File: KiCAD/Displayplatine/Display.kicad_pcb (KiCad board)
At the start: 2 copper layers, 14 parts, among them P1 CONN_01X08

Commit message: Displayplatine fertig + EADOG Footprint korrigiert
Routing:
- net GND: track 0.00 -> 267.9 mm
- net VCC: track 0.00 -> 93.5 mm
- net D5: track 0.00 -> 67.6 mm
- net D4: track 0.00 -> 67.6 mm
- net D3: track 0.00 -> 67.6 mm
- net D2: track 0.00 -> 67.6 mm
- net D1: track 0.00 -> 67.6 mm
- net Net-(C2-Pad1): track 0.00 -> 26.6 mm
- net LED: track 0.00 -> 24.4 mm
- net Net-(C5-Pad2): track 0.00 -> 19.2 mm
- net Net-(C7-Pad2): track 0.00 -> 14.1 mm
- net Net-(C3-Pad2): track 0.00 -> 13.6 mm
- net Net-(C1-Pad2): track 0.00 -> 13.6 mm
- net Net-(C2-Pad2): track 0.00 -> 12.2 mm
- net Net-(C6-Pad2): track 0.00 -> 11.7 mm
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
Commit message: nochmal
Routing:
- net VCC: track 93.5 -> 89.2 mm
- net GND: track 267.9 -> 266.5 mm
- added copper zone on B.Cu, net GND
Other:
- board outline added: 92.7 x 76.2 mm
- net class Default: trace_width 0.25 -> 0.3

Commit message: Displayplatine fertig
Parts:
- added P2: CONN_01X01, Pin_Headers:Pin_Header_Straight_1x01, F.Cu at (166.4, 123.2)
- added P3: CONN_01X01, Pin_Headers:Pin_Header_Straight_1x01, F.Cu at (166.4, 57.1)
- added P4: CONN_01X01, Pin_Headers:Pin_Header_Straight_1x01, F.Cu at (81.3, 57.1)
- added P5: CONN_01X01, Pin_Headers:Pin_Header_Straight_1x01, F.Cu at (81.3, 123.2)
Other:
- board size 92.7 x 76.2 mm -> 92.7 x 73.7 mm
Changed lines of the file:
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@@
     (links 36)
     (no_connects 0)
-    (area 81.35051 58.094999 158.145 118.435002)
+    (area 77.394999 53.264999 170.255001 127.075001)
     (thickness 1.6)
     (drawings 5)
     (tracks 115)
     (zones 0)
-    (modules 14)
-    (nets 23)
+    (modules 18)
+    (nets 27)
   )
   (page A4)
@@
   (net 21 D4)
   (net 22 LED)
+  (net 23 "Net-(P2-Pad1)")
+  (net 24 "Net-(P3-Pad1)")
+  (net 25 "Net-(P4-Pad1)")
+  (net 26 "Net-(P5-Pad1)")
   (net_class Default "Dies ist die voreingestellte Netzklasse."
     (clearance 0.2)
@@
     (add_net "Net-(D1-Pad2)")
     (add_net "Net-(D1-Pad3)")
+    (add_net "Net-(P2-Pad1)")
+    (add_net "Net-(P3-Pad1)")
+    (add_net "Net-(P4-Pad1)")
+    (add_net "Net-(P5-Pad1)")
     (add_net VCC)
   )
@@
       (net 1 GND))
   )
-  (gr_line (start 77.47 50.8) (end 170.18 50.8) (angle 90) (layer Edge.Cuts) (width 0.15))
+  (module Pin_Headers:Pin_Header_Straight_1x01 (layer F.Cu)
+    (at 166.37 123.19)
+    (descr "Through hole pin header")
+    (tags "pin header")
+    (fp_text reference P2 (at 0 -5.1) (layer F.SilkS)
+      (effects (font (size 1 1) (thickness 0.15)))
+    )
+    (fp_text value CONN_01X01 (at 0 -3.1) (layer F.Fab)
+      (effects (font (size 1 1) (thickness 0.15)))
+    )
+    (fp_line (start 1.55 -1.55) (end 1.55 0) (layer F.SilkS) (width 0.15))
+    (fp_line (start -1.75 -1.75) (end -1.75 1.75) (layer F.CrtYd) (width 0.05))
+    (fp_line (start 1.75 -1.75) (end 1.75 1.75) (layer F.CrtYd) (width 0.05))
+    (fp_line (start -1.75 -1.75) (end 1.75 -1.75) (layer F.CrtYd) (width 0.05))
+    (fp_line (start -1.75 1.75) (end 1.75 1.75) (layer F.CrtYd) (width 0.05))
+    (fp_line (start -1.55 0) (end -1.55 -1.55) (layer F.SilkS) (width 0.15))
+    (fp_line (start -1.55 -1.55) (end 1.55 -1.55) (layer F.SilkS) (width 0.15))
+    (fp_line (start -1.27 1.27) (end 1.27 1.27) (layer F.SilkS) (width 0.15))
+    (pad 1 thru_hole rect (at 0 0) (size 2.2352 2.2352) (drill 1.016) (layers *.Cu *.Mask F.SilkS)
+      (net 23 "Net-(P2-Pad1)"))
+    (model Pin_Headers.3dshapes/Pin_Header_Straight_1x01.wrl
+      (at (xyz 0 0 0))
+      (scale (xyz 1 1 1))
+      (rotate (xyz 0 0 90))
+    )
+  )
+  (module Pin_Headers:Pin_Header_Straight_1x01 (layer F.Cu)
+    (at 166.37 57.15)
+    (descr "Through hole pin header")
+    (tags "pin header")
+    (fp_text reference P3 (at 0 -5.1) (layer F.SilkS)
+      (effects (font (size 1 1) (thickness 0.15)))
+    )
+    (fp_text value CONN_01X01 (at 0 -3.1) (layer F.Fab)
+      (effects (font (size 1 1) (thickness 0.15)))
+    )
+    (fp_line (start 1.55 -1.55) (end 1.55 0) (layer F.SilkS) (width 0.15))
+    (fp_line (start -1.75 -1.75) (end -1.75 1.75) (layer F.CrtYd) (width 0.05))
+    (fp_line (start 1.75 -1.75) (end 1.75 1.75) (layer F.CrtYd) (width 0.05))
+    (fp_line (start -1.75 -1.75) (end 1.75 -1.75) (layer F.CrtYd) (width 0.05))
+    (fp_line (start -1.75 1.75) (end 1.75 1.75) (layer F.CrtYd) (width 0.05))
+    (fp_line (start -1.55 0) (end -1.55 -1.55) (layer F.SilkS) (width 0.15))
+    (fp_line (start -1.55 -1.55) (end 1.55 -1.55) (layer F.SilkS) (width 0.15))
+    (fp_line (start -1.27 1.27) (end 1.27 1.27) (layer F.SilkS) (width 0.15))
+    (pad 1 thru_hole rect (at 0 0) (size 2.2352 2.2352) (drill 1.016) (layers *.Cu *.Mask F.SilkS)
+      (net 24 "Net-(P3-Pad1)"))
+    (model Pin_Headers.3dshapes/Pin_Header_Straight_1x01.wrl
+      (at (xyz 0 0 0))
+      (scale (xyz 1 1 1))
+      (rotate (xyz 0 0 90))
+    )
+  )
+  (module Pin_Headers:Pin_Header_Straight_1x01 (layer F.Cu)
+    (at 81.28 57.15)
+    (descr "Through hole pin header")
+    (tags "pin header")
+    (fp_text reference P4 (at 0 -5.1) (layer F.SilkS)
+      (effects (font (size 1 1) (thickness 0.15)))
+    )
+    (fp_text value CONN_01X01 (at 0 -3.1) (layer F.Fab)
+      (effects (font (size 1 1) (thickness 0.15)))
+    )
+    (fp_line (start 1.55 -1.55) (end 1.55 0) (layer F.SilkS) (width 0.15))
+    (fp_line (start -1.75 -1.75) (end -1.75 1.75) (layer F.CrtYd) (width 0.05))
+    (fp_line (start 1.75 -1.75) (end 1.75 1.75) (layer F.CrtYd) (width 0.05))
+    (fp_line (start -1.75 -1.75) (end 1.75 -1.75) (layer F.CrtYd) (width 0.05))
+    (fp_line (start -1.75 1.75) (end 1.75 1.75) (layer F.CrtYd) (width 0.05))
+    (fp_line (start -1.55 0) (end -1.55 -1.55) (layer F.SilkS) (width 0.15))
+    (fp_line (start -1.55 -1.55) (end 1.55 -1.55) (layer F.SilkS) (width 0.15))
+    (fp_line (start -1.27 1.27) (end 1.27 1.27) (layer F.SilkS) (width 0.15))
+    (pad 1 thru_hole rect (at 0 0) (size 2.2352 2.2352) (drill 1.016) (layers *.Cu *.Mask F.SilkS)
+      (net 25 "Net-(P4-Pad1)"))
+    (model Pin_Headers.3dshapes/Pin_Header_Straight_1x01.wrl
+      (at (xyz 0 0 0))
+      (scale (xyz 1 1 1))
+      (rotate (xyz 0 0 90))
+    )
+  )
+  (module Pin_Headers:Pin_Header_Straight_1x01 (layer F.Cu)
+    (at 81.28 123.19)
+    (descr "Through hole pin header")
+    (tags "pin header")
+    (fp_text reference P5 (at 0 -5.1) (layer F.SilkS)
+      (effects (font (size 1 1) (thickness 0.15)))
+    )
+    (fp_text value CONN_01X01 (at 0 -3.1) (layer F.Fab)
+      (effects (font (size 1 1) (thickness 0.15)))
+    )
+    (fp_line (start 1.55 -1.55) (end 1.55 0) (layer F.SilkS) (width 0.15))
+    (fp_line (start -1.75 -1.75) (end -1.75 1.75) (layer F.CrtYd) (width 0.05))
+    (fp_line (start 1.75 -1.75) (end 1.75 1.75) (layer F.CrtYd) (width 0.05))
+    (fp_line (start -1.75 -1.75) (end 1.75 -1.75) (layer F.CrtYd) (width 0.05))
+    (fp_line (start -1.75 1.75) (end 1.75 1.75) (layer F.CrtYd) (width 0.05))
+    (fp_line (start -1.55 0) (end -1.55 -1.55) (layer F.SilkS) (width 0.15))
+    (fp_line (start -1.55 -1.55) (end 1.55 -1.55) (layer F.SilkS) (width 0.15))
+    (fp_line (start -1.27 1.27) (end 1.27 1.27) (layer F.SilkS) (width 0.15))
+    (pad 1 thru_hole rect (at 0 0) (size 2.2352 2.2352) (drill 1.016) (layers *.Cu *.Mask F.SilkS)
+      (net 26 "Net-(P5-Pad1)"))
+    (model Pin_Headers.3dshapes/Pin_Header_Straight_1x01.wrl
+      (at (xyz 0 0 0))
+      (scale (xyz 1 1 1))
+      (rotate (xyz 0 0 90))
+    )
+  )
+  (gr_line (start 77.47 53.34) (end 77.47 127) (angle 90) (layer Edge.Cuts) (width 0.15))
+  (gr_line (start 170.18 53.34) (end 170.18 71.12) (angle 90) (layer Edge.Cuts) (width 0.15))
+  (gr_line (start 77.47 53.34) (end 170.18 53.34) (angle 90) (layer Edge.Cuts) (width 0.15))
   (gr_line (start 77.47 127) (end 170.18 127) (angle 90) (layer Edge.Cuts) (width 0.15))
-  (gr_line (start 77.47 50.8) (end 77.47 127) (angle 90) (layer Edge.Cuts) (width 0.15))
-  (gr_line (start 170.18 50.8) (end 170.18 71.12) (angle 90) (layer Edge.Cuts) (width 0.15))
   (gr_line (start 170.18 71.12) (end 170.18 127) (angle 90) (layer Edge.Cuts) (width 0.15))
   (segment (start 153.67 66.04) (end 153.67 64.77) (width 0.3) (layer B.Cu) (net 1))

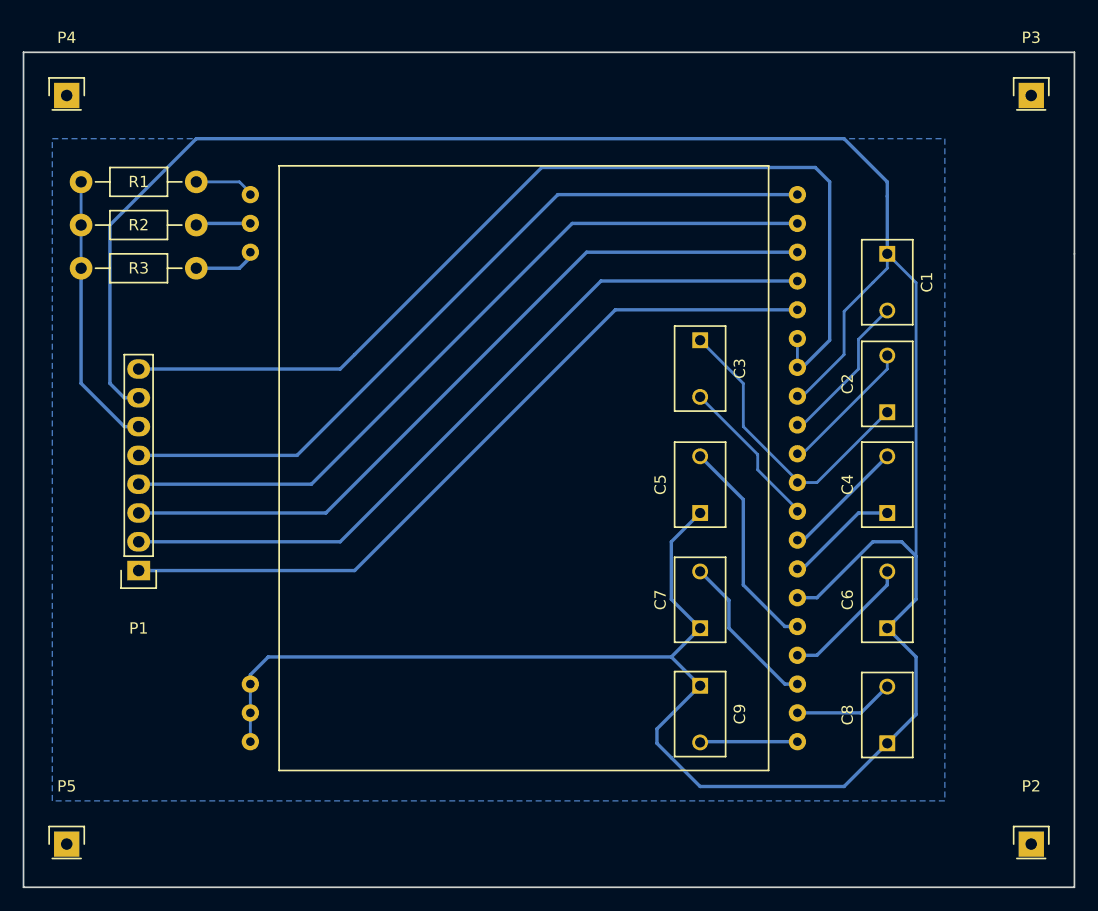
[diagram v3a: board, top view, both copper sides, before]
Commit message: Doku fortgesetzt, Platine wurde hergestellt
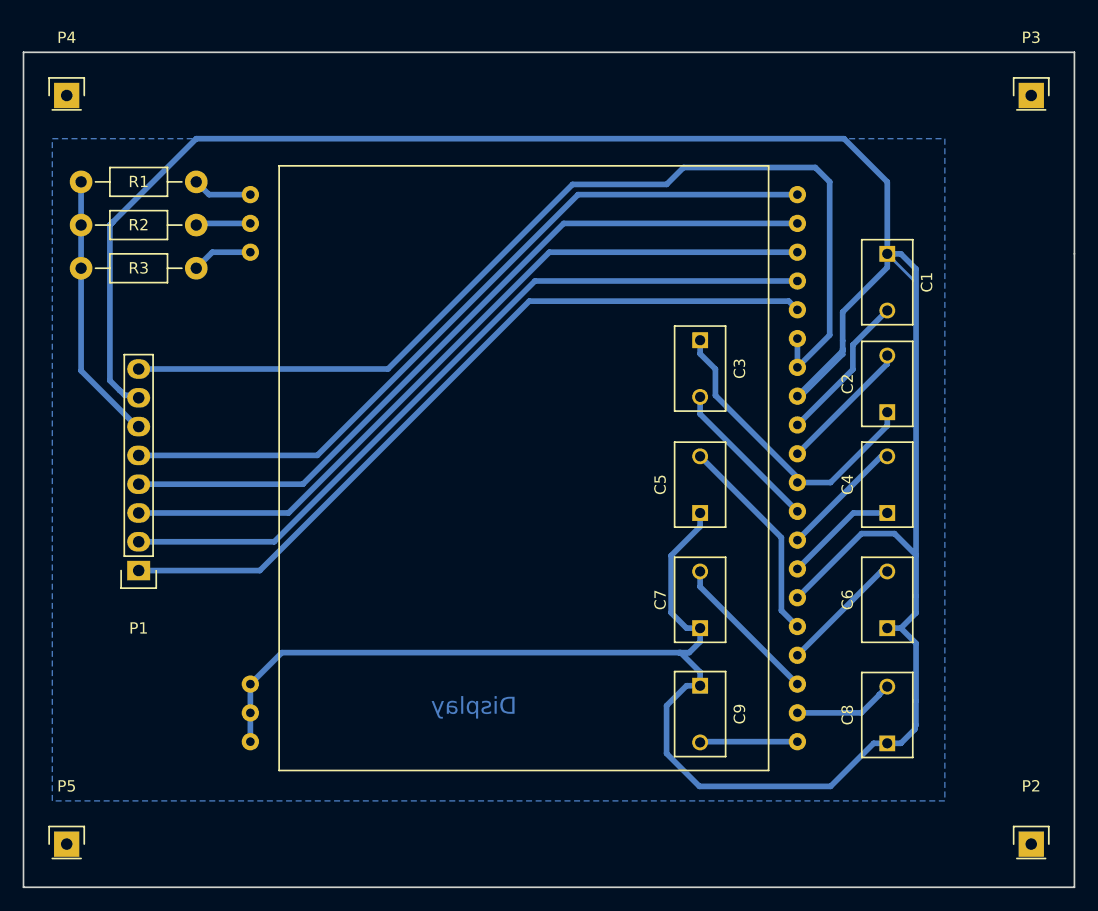
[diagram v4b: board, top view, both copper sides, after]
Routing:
- net GND: track 266.5 -> 317.7 mm
- net Net-(C2-Pad1): track 26.6 -> 27.3 mm
- net Net-(C6-Pad2): track 11.7 -> 11.0 mm
- net LED: track 24.4 -> 23.8 mm
- net Net-(C7-Pad2): track 14.1 -> 13.5 mm
- net Net-(C5-Pad2): track 19.2 -> 18.6 mm
- net D1: track 67.6 -> 68.3 mm
- net Net-(C4-Pad2): track 11.0 -> 11.5 mm
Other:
- net class Default: clearance 0.2 -> 0.4; via_dia 0.6 -> 1.5; via_drill 0.4 -> 0.9
- rule trace_clearance: 0.2 -> 0.4
- board text added: "Display"
